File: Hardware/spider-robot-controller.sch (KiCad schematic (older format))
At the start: 43 parts, among them CON1 AVR-ISP-6, CON2 BARREL_JACK, IC1 ATMEGA328-P, P1 SERVO_HEADER, P10 SERVO_HEADER, P11 SERVO_HEADER, P12 SERVO_HEADER, P13 Bluetooth_header, P14 CONN_01X01, P15 CONN_01X01, P16 CONN_01X01, P17 CONN_01X01, P18 CONN_01X01, P19 CONN_01X01, P2 SERVO_HEADER, P20 CONN_01X01, P21 CONN_01X01, P22 CONN_01X01, P23 CONN_01X01, P24 CONN_01X01, P25 CONN_01X01, P26 CONN_01X01, P27 CONN_01X01, P3 SERVO_HEADER, P4 SERVO_HEADER, P5 SERVO_HEADER, P6 SERVO_HEADER, P7 SERVO_HEADER, P8 SERVO_HEADER, P9 SERVO_HEADER, SW1 SW_PUSH, SW2 SWITCH_INV, U1 LM7805, Y1 16MHz

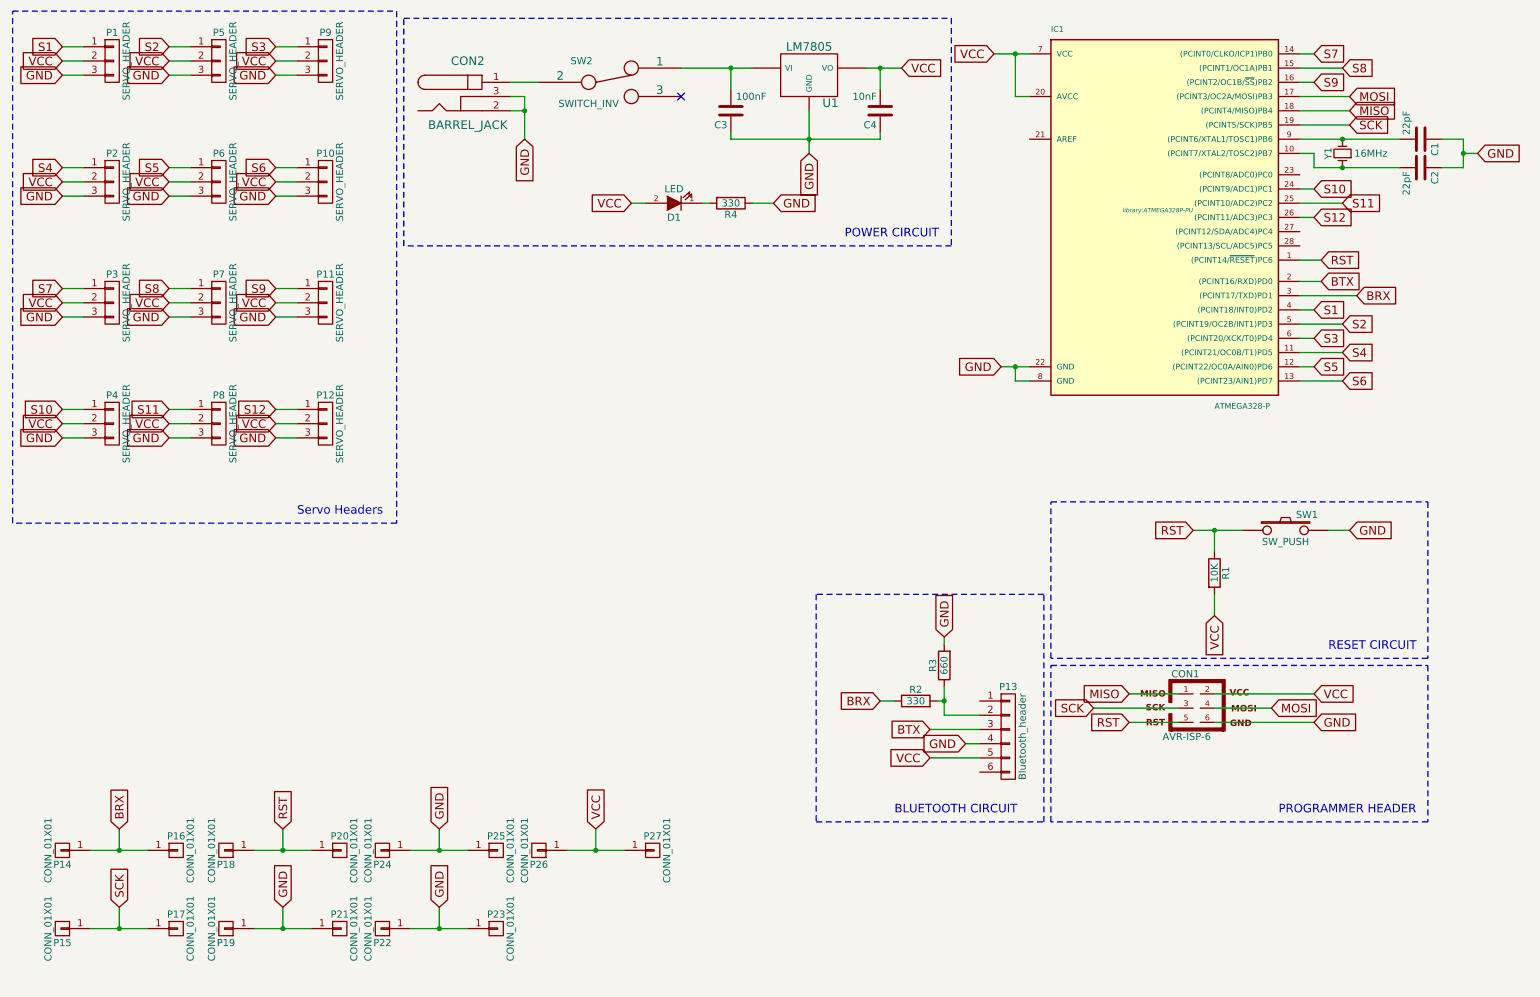
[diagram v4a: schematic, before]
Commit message: Changed from single board to a shield
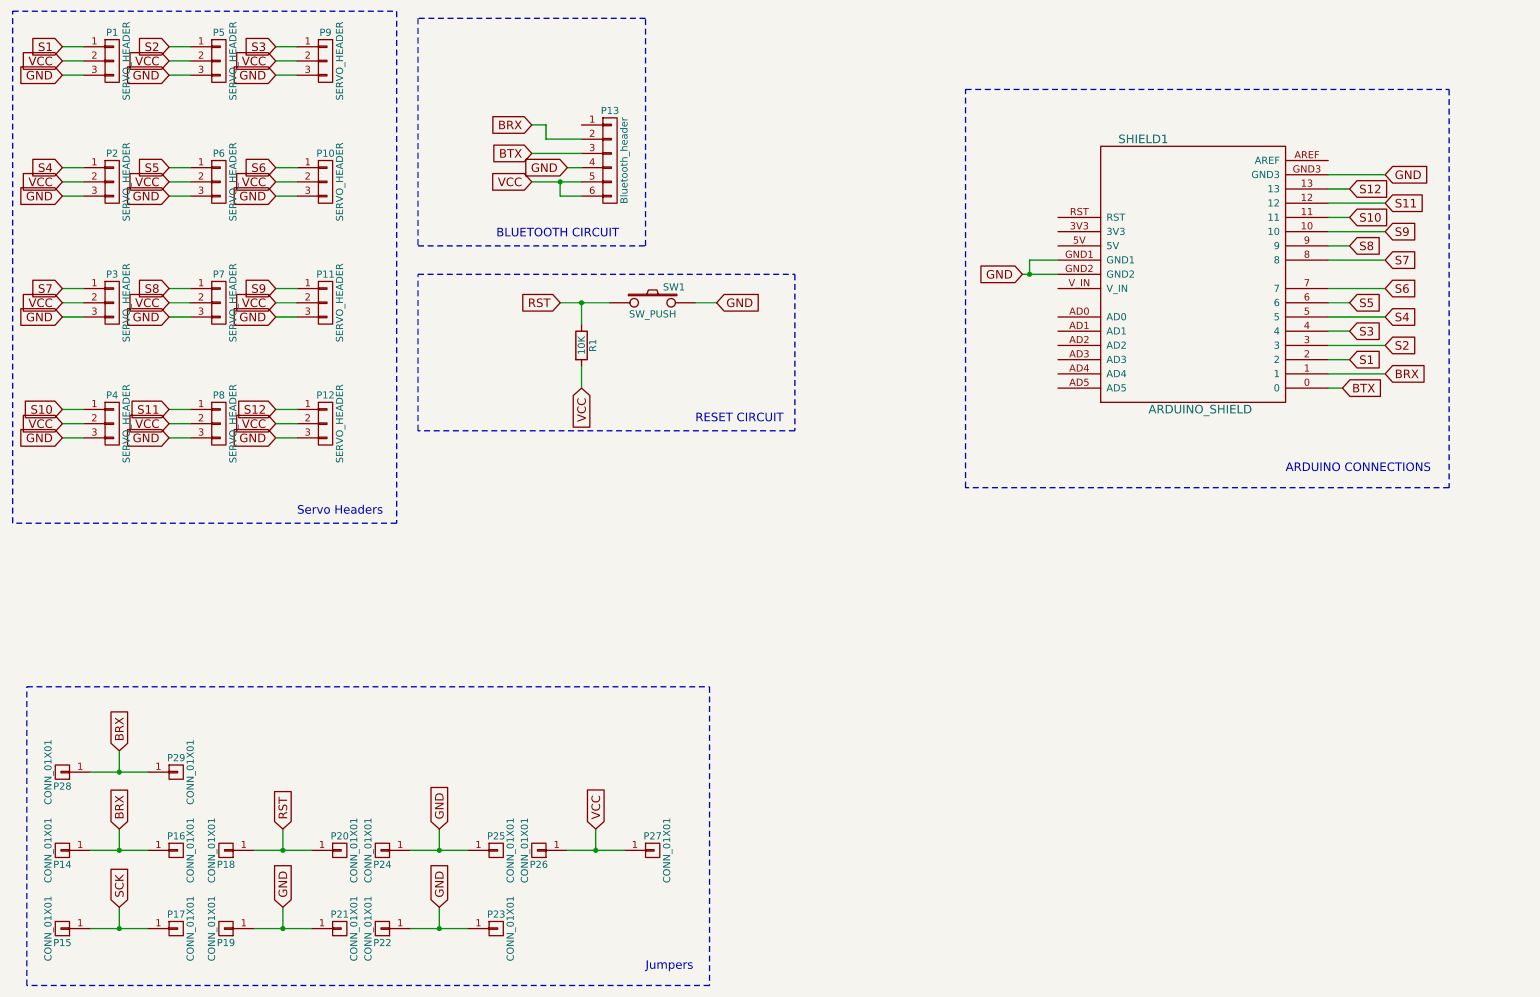
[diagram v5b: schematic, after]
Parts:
- removed C1, C2: 22pF, Capacitors_ThroughHole:C_Disc_D3_P2.5, symbol C
- removed C3: 100nF, Capacitors_ThroughHole:C_Radial_D10_L13_P5, symbol C
- removed C4: 10nF, Capacitors_ThroughHole:C_Radial_D5_L6_P2.5, symbol C
- removed CON1: AVR-ISP-6, Pin_Headers:Pin_Header_Straight_2x03, symbol AVR-ISP-6
- removed CON2: BARREL_JACK, library:BARREL_JACK, symbol BARREL_JACK
- removed D1: LED, LEDs:LED-5MM, symbol LED
- removed IC1: ATMEGA328-P, library:ATMEGA328P-PU, symbol ATMEGA328-P
- removed R2, R4: 330, Resistors_ThroughHole:Resistor_Horizontal_RM10mm, symbol R
- removed R3: 660, Resistors_ThroughHole:Resistor_Horizontal_RM10mm, symbol R
- removed SW2: SWITCH_INV, library:SWITCH_INVERTER, symbol SWITCH_INV
- removed U1: LM7805, library:LM7805, symbol LM7805
- removed Y1: 16MHz, Crystals:Crystal_HC49-U_Vertical, symbol Crystal_Small
- added P28, P29: CONN_01X01, Pin_Headers:Pin_Header_Straight_1x01, symbol CONN_01X01
- added SHIELD1: ARDUINO_SHIELD, freetronics_footprints:ARDUINO_SHIELD_ROUNDPADS, symbol ARDUINO_SHIELD
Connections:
- net BRX: now also P13.2 (P2), P28.1 (P1), P29.1 (P1), SHIELD1.1
- net BTX: now also SHIELD1.0
- net GND: now also SHIELD1.GND1, SHIELD1.GND2, SHIELD1.GND3
- net S1: now also SHIELD1.2
- net S10: now also SHIELD1.11
- net S11: now also SHIELD1.12
- net S12: now also SHIELD1.13
- net S2: now also SHIELD1.3
- net S3: now also SHIELD1.4
- net S4: now also SHIELD1.5
- net S5: now also SHIELD1.6
- net S6: now also SHIELD1.7
- net S7: now also SHIELD1.8
- net S8: now also SHIELD1.9
- net S9: now also SHIELD1.10
- net VCC: now also P13.6 (P6)
- no-connect marks 1 -> 0
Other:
- note added: "ARDUINO CONNECTIONS"
- note added: "Jumpers"
- note removed: "POWER CIRCUIT"
- note removed: "PROGRAMMER HEADER"
- moved on the sheet: P13, R1, SW1

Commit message: Improvements on the shield
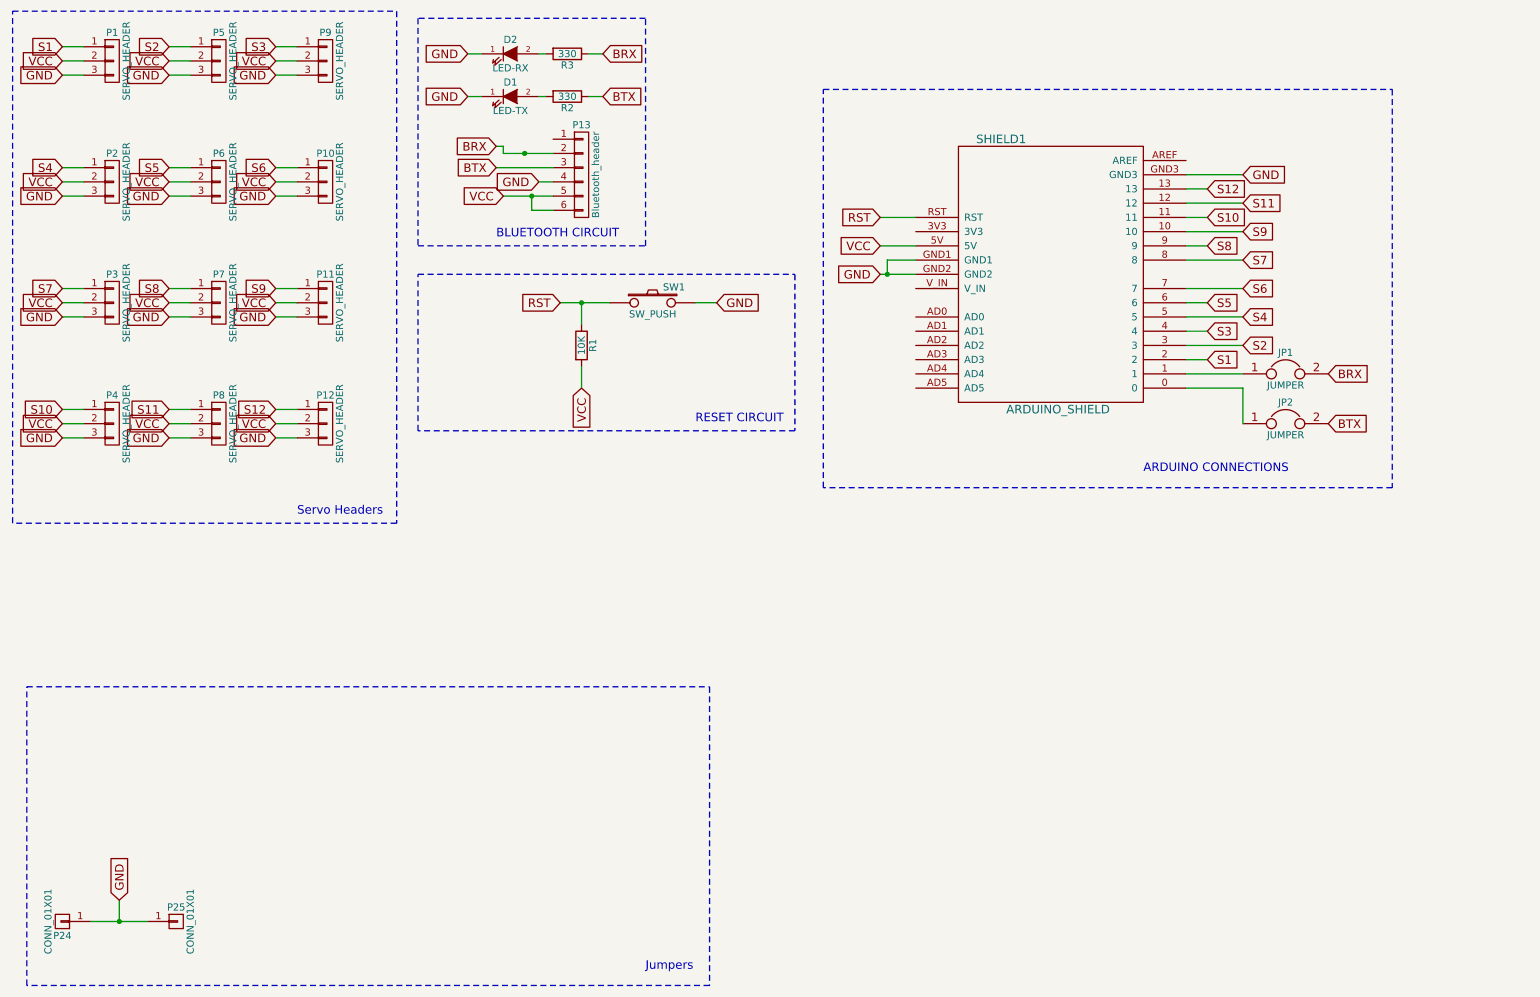
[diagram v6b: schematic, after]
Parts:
- removed P14, P15, P16, P17, P18, P19, P20, P21, P22, P23, P26, P27, P28, P29: CONN_01X01, Pin_Headers:Pin_Header_Straight_1x01, symbol CONN_01X01
- added D1: LED-TX, LEDs:LED-5MM, symbol LED
- added D2: LED-RX, LEDs:LED-5MM, symbol LED
- added JP1, JP2: JUMPER, Pin_Headers:Pin_Header_Straight_1x02, symbol JUMPER
- added R2, R3: 330, Resistors_ThroughHole:Resistor_Horizontal_RM15mm, symbol R
- P13: footprint Pin_Headers:Pin_Header_Straight_1x06 -> Pin_Headers:Pin_Header_Angled_1x06
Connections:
- net BRX: now also JP1.2, R3.1; no longer SHIELD1.1
- net BTX: now also JP2.2, R2.1; no longer SHIELD1.0
- net GND: now also D1.1 (K), D2.1 (K)
- net RST: now also SHIELD1.RST
- net VCC: now also SHIELD1.5V
- new net: JP2.1, SHIELD1.0
- new net: JP1.1, SHIELD1.1
- new net: D2.2 (A), R3.2
- new net: D1.2 (A), R2.2
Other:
- moved on the sheet: P13, P24, P25, SHIELD1

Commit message: Improved layout of the board - BT module fits better
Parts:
- R2, R3: footprint Resistors_ThroughHole:Resistor_Horizontal_RM15mm -> Resistors_ThroughHole:Resistor_Horizontal_RM10mm
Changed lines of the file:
@@
 F 0 "R3" V 4580 850 50  0000 C CNN
 F 1 "330" V 4500 850 50  0000 C CNN
-F 2 "Resistors_ThroughHole:Resistor_Horizontal_RM15mm" V 4430 850 30  0001 C CNN
+F 2 "Resistors_ThroughHole:Resistor_Horizontal_RM10mm" V 4430 850 30  0001 C CNN
 F 3 "" H 4500 850 30  0000 C CNN
 	1    4500 850
@@
 F 0 "R2" V 4580 1150 50  0000 C CNN
 F 1 "330" V 4500 1150 50  0000 C CNN
-F 2 "Resistors_ThroughHole:Resistor_Horizontal_RM15mm" V 4430 1150 30  0001 C CNN
+F 2 "Resistors_ThroughHole:Resistor_Horizontal_RM10mm" V 4430 1150 30  0001 C CNN
 F 3 "" H 4500 1150 30  0000 C CNN
 	1    4500 1150

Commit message: updated gerbers
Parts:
- added P14, P15: CONN_01X01, Pin_Headers:Pin_Header_Straight_1x01, symbol CONN_01X01
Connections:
- net GND: now also P14.1 (P1), P15.1 (P1)
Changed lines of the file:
@@
 Wire Wire Line
 	4750 1150 4650 1150
+$Comp
+L CONN_01X01 P15
+U 1 1 5644BF11
+P 1750 6250
+F 0 "P15" H 1750 6350 50  0000 C CNN
+F 1 "CONN_01X01" V 1850 6250 50  0000 C CNN
+F 2 "Pin_Headers:Pin_Header_Straight_1x01" H 1750 6250 60  0001 C CNN
+F 3 "" H 1750 6250 60  0000 C CNN
+	1    1750 6250
+	1    0    0    -1
+$EndComp
+$Comp
+L CONN_01X01 P14
+U 1 1 5644BF17
+P 950 6250
+F 0 "P14" H 950 6350 50  0000 C CNN
+F 1 "CONN_01X01" V 1050 6250 50  0000 C CNN
+F 2 "Pin_Headers:Pin_Header_Straight_1x01" H 950 6250 60  0001 C CNN
+F 3 "" H 950 6250 60  0000 C CNN
+	1    950  6250
+	-1   0    0    1
+$EndComp
+Text GLabel 1350 6100 1    60   Input ~ 0
+GND
+Wire Wire Line
+	1150 6250 1550 6250
+Wire Wire Line
+	1350 6250 1350 6100
+Connection ~ 1350 6250
 $EndSCHEMATC
